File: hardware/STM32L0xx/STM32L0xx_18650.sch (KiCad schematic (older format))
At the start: 53 parts, among them J2 Battery, J3 GPIO, J4 USB_B_Micro, J5 Power, J6 LEDs, J7 GPIO, Q1 BSS806N, Q2 BSS806N, Q3 BSS806N, Q4 BSS806N, SW1 Mode, SW2 Power, U1 STM32L072KZTx, U2 AP2210N-3.3TRG1, U3 BQ21040, U4 ESD7002WTT1G, Y1 32.768kHz

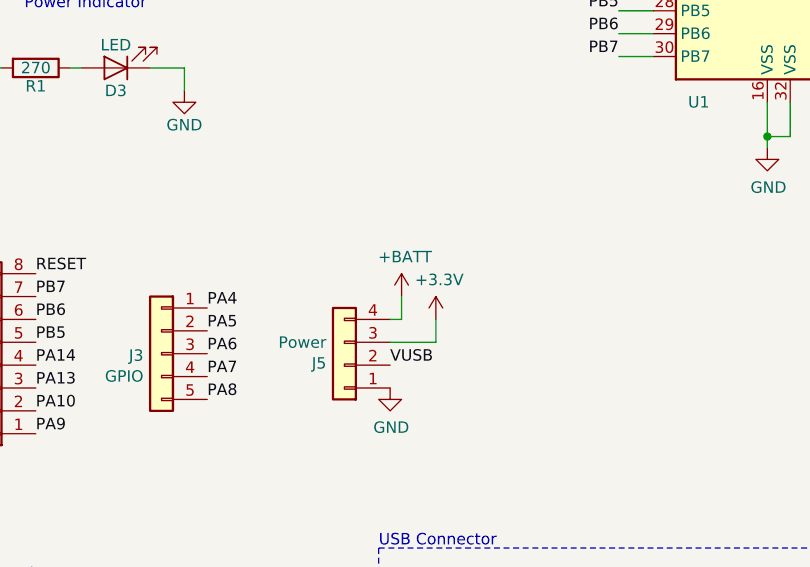
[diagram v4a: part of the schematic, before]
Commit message: Change BATT+ to Vin
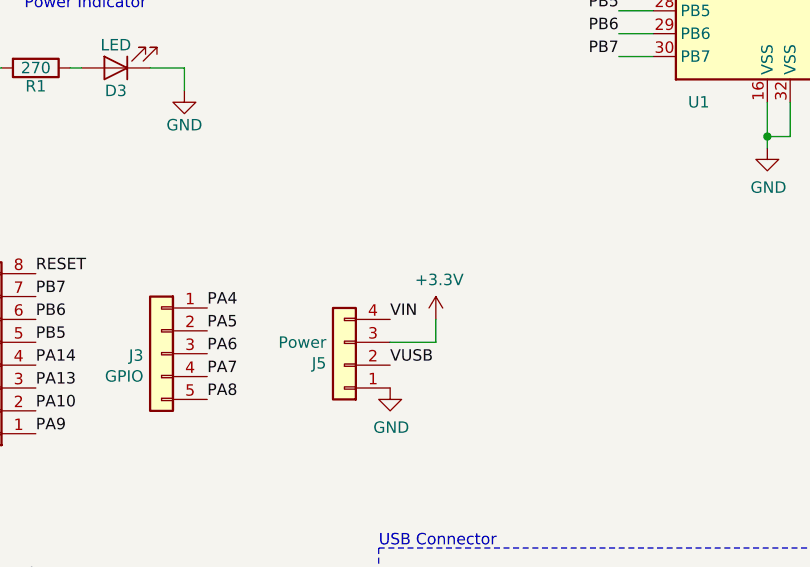
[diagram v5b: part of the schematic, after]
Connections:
- net +BATT: no longer J5.4 (Pin_4)
- net VIN: now also J5.4 (Pin_4)
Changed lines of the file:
@@
 	2750 5350 2750 5450
-$Comp
-L power:+BATT #PWR?
-U 1 1 5C2E47A9
-P 2600 5250
-AR Path="/5BD64BD8/5C2E47A9" Ref="#PWR?"  Part="1"
-AR Path="/5C2E47A9" Ref="#PWR0131"  Part="1"
-F 0 "#PWR0131" H 2600 5100 50  0001 C CNN
-F 1 "+BATT" H 2615 5423 50  0000 C CNN
-F 2 "" H 2600 5250 50  0001 C CNN
-F 3 "" H 2600 5250 50  0001 C CNN
-	1    2600 5250
-	1    0    0    -1
-$EndComp
-Wire Wire Line
-	2600 5350 2550 5350
-Wire Wire Line
-	2600 5250 2600 5350
 $Comp
 L power:+3.3V #PWR0130
@@
 Wire Wire Line
 	9850 5050 10050 5050
+Text Label 2550 5350 0    50   ~ 0
+VIN
 $EndSCHEMATC

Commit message: Update charge indicator LED
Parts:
- D6: MPN 150060VS75000 -> 150060BS55040
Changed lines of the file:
@@
 F 2 "LED_SMD:LED_0603_1608Metric" H 9900 5850 50  0001 C CNN
 F 3 "" H 9900 5850 50  0001 C CNN
-F 4 "150060VS75000" H 9900 5850 50  0001 C CNN "MPN"
+F 4 "150060BS55040" H 9900 5850 50  0001 C CNN "MPN"
 F 5 "0603" H 800 1000 50  0001 C CNN "Package"
 	1    9900 5850
